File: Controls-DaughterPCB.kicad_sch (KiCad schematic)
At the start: 23 parts, among them U8 LMC555xM

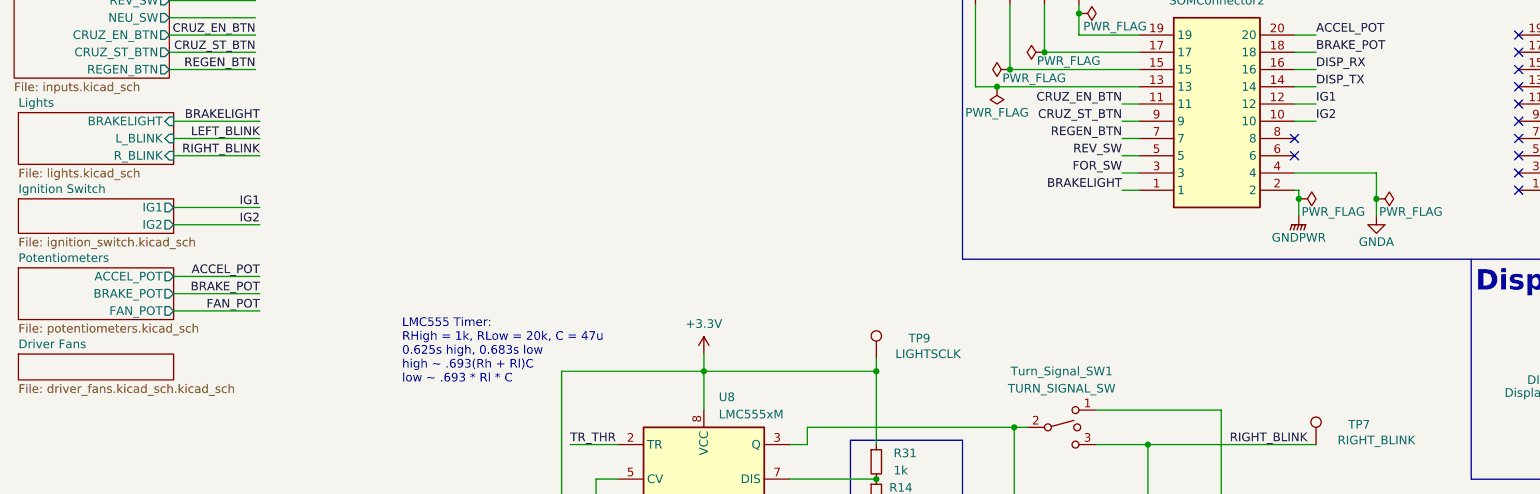
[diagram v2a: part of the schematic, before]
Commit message: Added drived fan circuitry
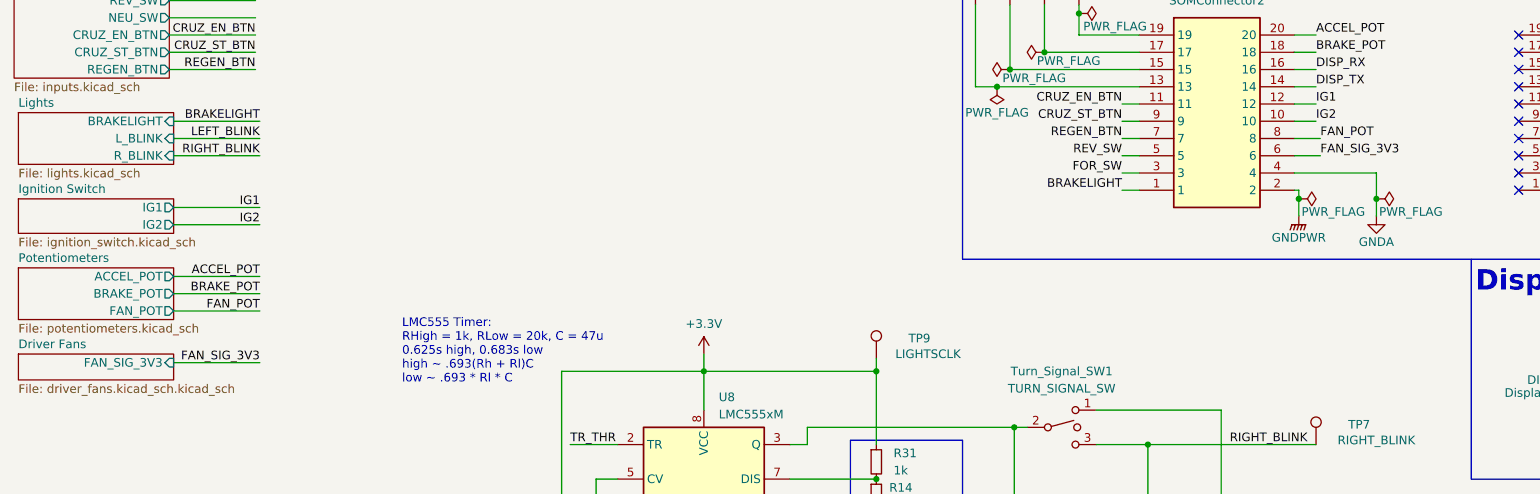
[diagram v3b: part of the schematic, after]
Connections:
- net FAN_POT: now also SOM1.8
- net FAN_SIG_3V3: now reaches SOM1.6
- no-connect marks 22 -> 20
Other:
- sheet Driver Fans ports: added FAN_SIG_3V3; removed none
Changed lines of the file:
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@@
   (no_connect (at 242.57 38.1))
   (no_connect (at 265.43 40.64))
-  (no_connect (at 209.55 50.8))
   (no_connect (at 265.43 43.18))
-  (no_connect (at 209.55 48.26))
   (no_connect (at 242.57 50.8))
   (polyline (pts (xy 144.145 92.71) (xy 160.655 92.71))
@@
     (stroke (width 0) (type default))
   )
+  (wire (pts (xy 209.55 50.8) (xy 213.36 50.8))
+    (stroke (width 0) (type default))
+  )
   (wire (pts (xy 109.855 98.425) (xy 106.68 98.425))
     (stroke (width 0) (type default))
@@
     (stroke (width 0) (type default))
   )
+  (wire (pts (xy 209.55 48.26) (xy 213.36 48.26))
+    (stroke (width 0) (type default))
+  )
   (wire (pts (xy 184.15 48.26) (xy 186.69 48.26))
     (stroke (width 0) (type default))
@@
   )
   (wire (pts (xy 210.185 55.88) (xy 210.185 57.15))
+    (stroke (width 0) (type default))
+  )
+  (wire (pts (xy 44.45 81.28) (xy 57.15 81.28))
     (stroke (width 0) (type default))
   )
@@
     (effects (font (size 1.27 1.27)) (justify right bottom))
   )
+  (label "FAN_POT" (at 213.36 48.26 0) (fields_autoplaced)
+    (effects (font (size 1.27 1.27)) (justify left bottom))
+  )
   (label "LEFT_BLINK" (at 211.455 105.41 180) (fields_autoplaced)
     (effects (font (size 1.27 1.27)) (justify right bottom))
@@
     (effects (font (size 1.27 1.27)) (justify left bottom))
   )
+  (label "FAN_SIG_3V3" (at 213.36 50.8 0) (fields_autoplaced)
+    (effects (font (size 1.27 1.27)) (justify left bottom))
+  )
   (label "BRAKELIGHT" (at 184.15 55.88 180) (fields_autoplaced)
     (effects (font (size 1.27 1.27)) (justify right bottom))
@@
   (label "CRUZ_ST_BTN" (at 56.515 35.56 180) (fields_autoplaced)
     (effects (font (size 1.23 1.23)) (justify right bottom))
+  )
+  (label "FAN_SIG_3V3" (at 57.15 81.28 180) (fields_autoplaced)
+    (effects (font (size 1.27 1.27)) (justify right bottom))
   )
   (label "DISP_TX" (at 212.725 40.64 0) (fields_autoplaced)
@@
       (effects (font (size 1.27 1.27)) (justify left top))
     )
-    (instances
+    (pin "FAN_SIG_3V3" input (at 44.45 81.28 0)
+      (effects (font (size 1.27 1.27)) (justify right))
+    )
+    (instances

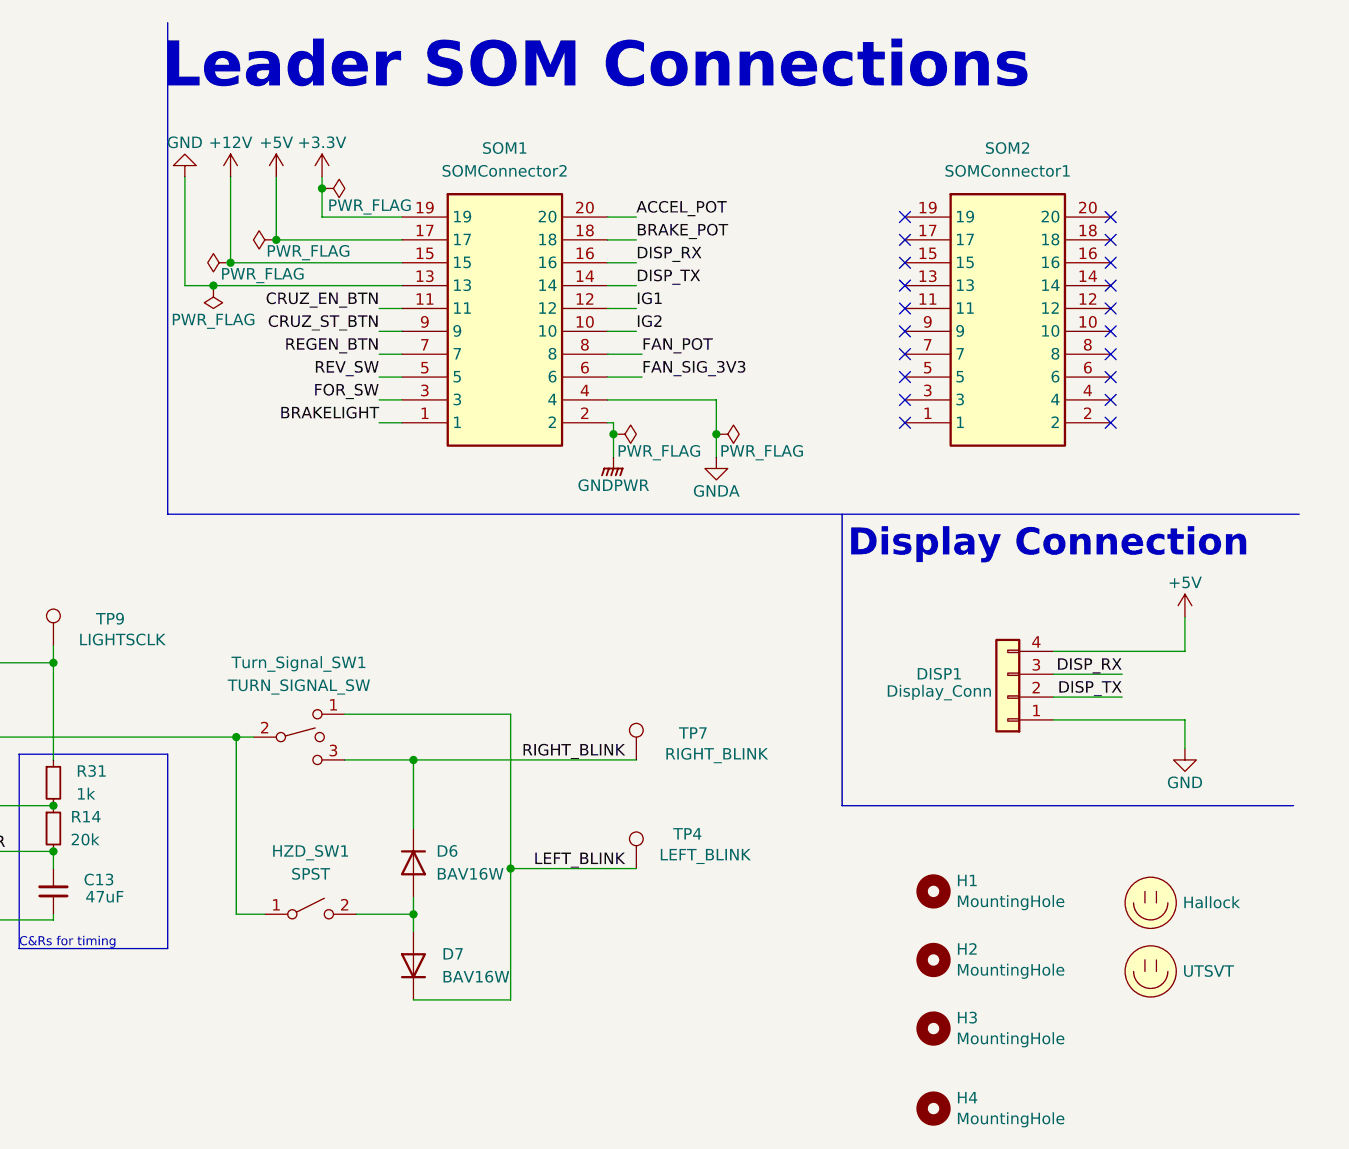
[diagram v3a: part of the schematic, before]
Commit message: Added resistor to fan isolator, fixed ERC errors and warnings
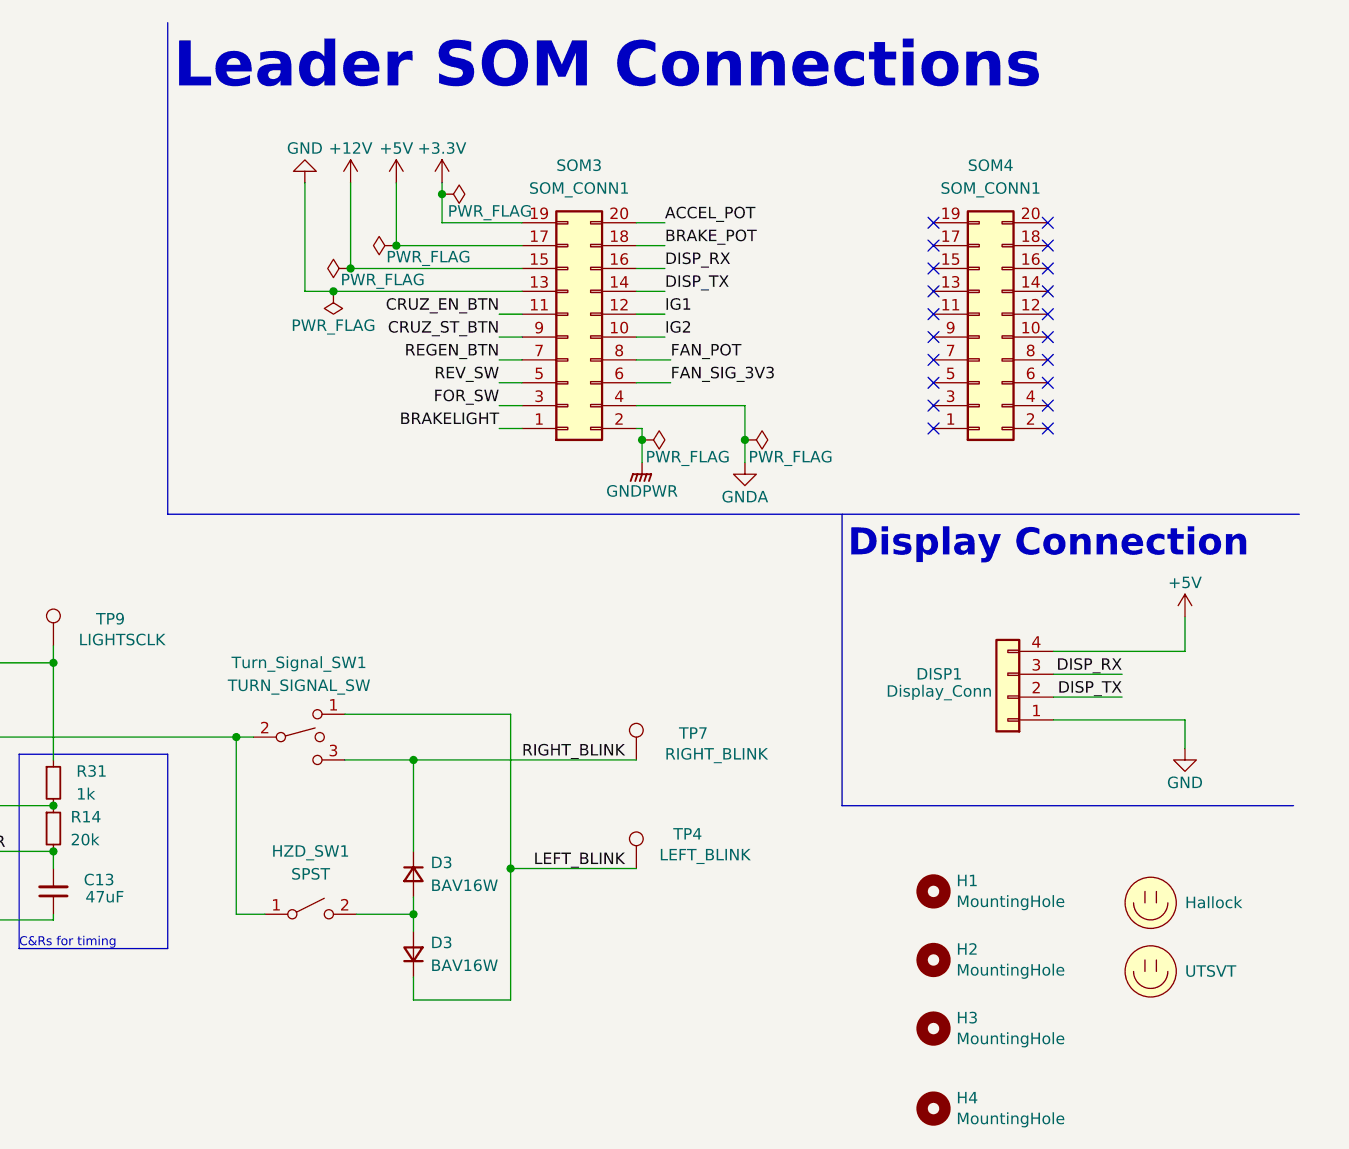
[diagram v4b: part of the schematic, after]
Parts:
- removed D6, D7: BAV16W, Diode_SMD:D_SOD-123, symbol Diode:BAV16W
- removed LOGO2: UTSVT, UTSVT_Special:UTSVT_Logo_Symbol, symbol utsvt-misc:Logo_Placeholder
- removed SOM1: SOMConnector2, UTSVT_Connectors:Molex_52465-2070, symbol utsvt-connectors:SOMConnector
- removed SOM2: SOMConnector1, UTSVT_Connectors:Molex_52465-2070, symbol utsvt-connectors:SOMConnector
- added D3 (x2): BAV16W, Diode_SMD:D_SOD-123, symbol Device:D_Small
- added LOGO3: Hallock, UTSVT_Special:Hallock_Image_Small, symbol utsvt-misc:Logo_Placeholder
- added SOM3, SOM4: SOM_CONN1, UTSVT_Connectors:Molex_52465-2070, symbol Connector_Generic:Conn_02x10_Odd_Even
- LOGO1: value Hallock -> UTSVT; footprint UTSVT_Special:Hallock_Image_Small -> UTSVT_Special:UTSVT_Logo_Symbol
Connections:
- net +12V: now also SOM3.15 (Pin_15)
- net +3.3V: now also SOM3.19 (Pin_19)
- net +5V: now also SOM3.17 (Pin_17)
- net ACCEL_POT: now also SOM3.20 (Pin_20)
- net BRAKELIGHT: now also SOM3.1 (Pin_1)
- net BRAKE_POT: now also SOM3.18 (Pin_18)
- net CRUZ_EN_BTN: now also SOM3.11 (Pin_11)
- net CRUZ_ST_BTN: now also SOM3.9 (Pin_9)
- net DISP_RX: now also SOM3.16 (Pin_16)
- net DISP_TX: now also SOM3.14 (Pin_14)
- net FAN_POT: now also SOM3.8 (Pin_8)
- net FAN_SIG_3V3: now also SOM3.6 (Pin_6)
- net FOR_SW: now also SOM3.3 (Pin_3)
- net GND: now also SOM3.13 (Pin_13)
- net GNDA: now also SOM3.4 (Pin_4)
- net GNDPWR: now also SOM3.2 (Pin_2)
- net IG1: now also SOM3.12 (Pin_12)
- net IG2: now also SOM3.10 (Pin_10)
- net LEFT_BLINK: now also D3.1 (K)
- net REGEN_BTN: now also SOM3.7 (Pin_7)
- net REV_SW: now also SOM3.5 (Pin_5)
- net RIGHT_BLINK: now also D3.1 (K)
- net at HZD_SW1.2 (B): now also D3.2 (A), D3.2 (A)

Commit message: added version history text
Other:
- note added: "- find a more power effiecient optocoupler for ignition switch, and potentiallt a smaller optocoupler for lights which does not need a MOSFET."
- note added: "V1.0*"
- note added: "V1.1"
- note added: "Version History (* = current version)"
- note added: "controls head lights, break lights, internal & external blinkers, driver fans, ignition, forward, neutral, reverse, cruise control, and regen from inputs on the car. 12V is isolated from 3V3 and 5V using optocouplers. CMOS 555 timer used for blinkers."
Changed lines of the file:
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@@
     (stroke (width 0) (type default))
+  )
+  (rectangle (start 12.7 128.905) (end 175.895 196.85)
+    (stroke (width 0) (type default))
+    (fill (type none))
   )
   (text "C&Rs for timing" (at 144.145 114.3 0)
     (effects (font (size 1 1)) (justify left bottom))
   )
+  (text "V1.1" (at 13.335 142.875 0)
+    (effects (font (size 2 2) (thickness 0.4) bold) (justify left bottom))
+  )
   (text "Leader SOM Connections\n\n" (at 161.29 27.305 0)
     (effects (font (size 5 5) (thickness 0.7) bold) (justify left bottom))
+  )
+  (text "controls head lights, break lights, internal & external blinkers, driver fans, ignition, forward, neutral, reverse, cruise control, and regen from inputs on the car.\n12V is isolated from 3V3 and 5V using optocouplers. CMOS 555 timer used for blinkers."
+    (at 16.51 137.16 0)
+    (effects (font (size 1.27 1.27) bold) (justify left bottom))
+  )
+  (text "- find a more power effiecient optocoupler for ignition switch, and potentiallt a smaller optocoupler for lights which does not need a MOSFET."
+    (at 16.51 145.415 0)
+    (effects (font (size 1.27 1.27) bold) (justify left bottom))
+  )
+  (text "V1.0*" (at 13.335 132.715 0)
+    (effects (font (size 2 2) (thickness 0.4) bold) (justify left bottom))
   )
   (text "Display Connection\n" (at 236.22 71.12 0)
@@
     (effects (font (size 1.27 1.27)) (justify left bottom))
   )
+  (text "Version History (* = current version)" (at 12.065 127 0)
+    (effects (font (size 4 4) (thickness 0.8) bold) (justify left bottom))
+  )
   (label "REGEN_BTN" (at 56.515 38.1 180) (fields_autoplaced)
